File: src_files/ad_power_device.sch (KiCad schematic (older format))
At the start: 17 parts, among them J1 SPEAKER, J2 5622-6309-ML, Q1 DTC143ZEBTL, Q2 DTC143ZEBTL, U7 QUECTEL_L70-RL

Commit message: update NFC, 5G, GPS__left LiPo charger+screen changes
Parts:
- added C? (x3): 100nF, symbol Device:C_Small
- added C? (x2): 220pF, symbol Device:C_Small
- added C? (x2): 180pF, symbol Device:C_Small
- added C?: 66pF, symbol Device:C_Small
- added C?: 4.7uF, symbol Device:C_Small
- added J?: Conn_01x05_Male, symbol Connector:Conn_01x05_Male
- added J?: 205957-0271, 2059570271, symbol SamacSys_Parts:205957-0271
- added R? (x2): 0R, Resistor_SMD:R_0402_1005Metric, symbol Device:R_US
- added R? (x2): 4.7K, Resistor_SMD:R_0402_1005Metric, symbol Device:R_US
- added R?: 1K, Resistor_SMD:R_0402_1005Metric, symbol Device:R_US
- added U?: NFC_VS1797SM, greencharge-footprints:VS1797SM, symbol GCL_Integrated-Circuits:NFC_VS1797SM
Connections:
- net labels added: ANTRDR_n, ANTRDR_p, NFC_REQ, NFC_SCL, NFC_SDA, NFC_WAKE, PWM_IR, RF1, RF2, RX_IR, TX_IR, VCC3V3_PMU, VDDIO
- wire segments 189 -> 277
- no-connect marks 13 -> 18
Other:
- note added: "5G_RADAR_MODULE\n"
- note added: "ANTENNA CONNECTOR"
- note added: "I2C_PULLUP"
- note added: "NFC_IC_VS1797SM"
- note added: "NFC_MODULE SECTION"
- note added: "NOTE: accompanying NFC ANTENNA\n538-146236-2151\nlink: https://eu.mouser.com/ProductDetail/Molex/146236-2151?qs=xZ%2FP%252Ba9zWqYI0Z0ju1H6Kw%3D%3D"
- note added: "TO 5G RADA MODULE"
- note added: "https://www.hlktech.com/en/Product/Details/85"
- moved on the sheet: H1, H2, H3, H4

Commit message: schematic capture complete
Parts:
- removed AE2: Antenna, symbol Device:Antenna
- added C283: 100nF, Capacitor_SMD:C_0402_1005Metric, symbol Device:C_Small
- added J15: U.FL-R-SMT-1(10), greencharge-footprints:HRS_U.FL-R-SMT-1(10), symbol U.FL-R-SMT-1_10_:U.FL-R-SMT-1(10)
- C149, C150: footprint (none) -> Capacitor_SMD:C_0402_1005Metric
- C177, C178, C179, C180, C181, C182, C183, C184, C185: renamed from C?; footprint (none) -> Capacitor_SMD:C_0402_1005Metric
- D1, D2: footprint LED_SMD:LED_0402_1005Metric -> LED_SMD:LED_0201_0603Metric_Pad0.64x0.40mm_HandSolder
- J3: renamed from J?; footprint 2059570271 -> greencharge-footprints:2059570271
- J7: renamed from J?; footprint (none) -> Connector_PinHeader_2.54mm:PinHeader_1x05_P2.54mm_Vertical
- R28: footprint (none) -> Resistor_SMD:R_0402_1005Metric
- gave numbers to parts that had none: 6
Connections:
- net labels added: I2C0_SCL_PMIC, I2C0_SDA_PMIC, PMIC_EXT_EN, RECOVER, USB_OTG0_D+, USB_OTG0_D-, USB_OTG0_VBUSDET, VCC3V3_EXT
- net labels removed: VCC3V3_PMU
- wire segments 277 -> 308
- no-connect marks 18 -> 29
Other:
- note added: "RK3566 AND SUPPORTING COMPONENTS SECTION"
- note added: "USB_OTG AND POWER_INPUT"
- moved on the sheet: J1

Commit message: updated footprint and schematics
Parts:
- removed C149: 10uF, Capacitor_SMD:C_0402_1005Metric, symbol Device:C_Small
- removed C150, C283: 100nF, Capacitor_SMD:C_0402_1005Metric, symbol Device:C_Small
- removed D1, D2: LED, LED_SMD:LED_0201_0603Metric_Pad0.64x0.40mm_HandSolder, symbol Device:LED
- removed J15: U.FL-R-SMT-1(10), greencharge-footprints:HRS_U.FL-R-SMT-1(10), symbol U.FL-R-SMT-1_10_:U.FL-R-SMT-1(10)
- removed Q1, Q2: DTC143ZEBTL, greencharge-footprints:SOTFL50P160X85-3N, symbol DTC143ZEBTL:DTC143ZEBTL
- removed R28: 0R, Resistor_SMD:R_0402_1005Metric, symbol Device:R_US
- removed R29, R30: 1K, Resistor_SMD:R_0402_1005Metric, symbol Device:R_US
- removed U7: QUECTEL_L70-RL, greencharge-footprints:QUECTEL_L70-R, symbol GCL_Integrated-Circuits:QUECTEL_L70-R
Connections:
- net labels added: AP_READY
- net labels removed: +3V3, IPPS, STANDBY
- wire segments 308 -> 268
- no-connect marks 29 -> 23
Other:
- note added: "4G AND GPS_MODULE(COMPACT)\n"
- note added: "LINK TO DRIVE SATA TYPE: \nhttps://de.aliexpress.com/item/4001072133790.html?spm=a2g0o.detail.1000014.15.36804d48TZzJhy&gps-id=pcDetailBottomMoreOtherSeller&scm=1007.33416.213724.0&scm_id=1007.33416.213724.0&scm-url=1007.33416.213724.0&pvid=9e456f25-bf32-4544-9c19-67c56a9949ae&_t=gps-id:pcDetailBottomMoreOtherSeller,scm-url:1007.33416.213724.0,pvid:9e456f25-bf32-4544-9c19-67c56a9949ae,tpp_buckets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"
- note removed: "4G_MODULE\n"
- note removed: "GPS_MODULE"
- note removed: "Z0=50Ohm\n"

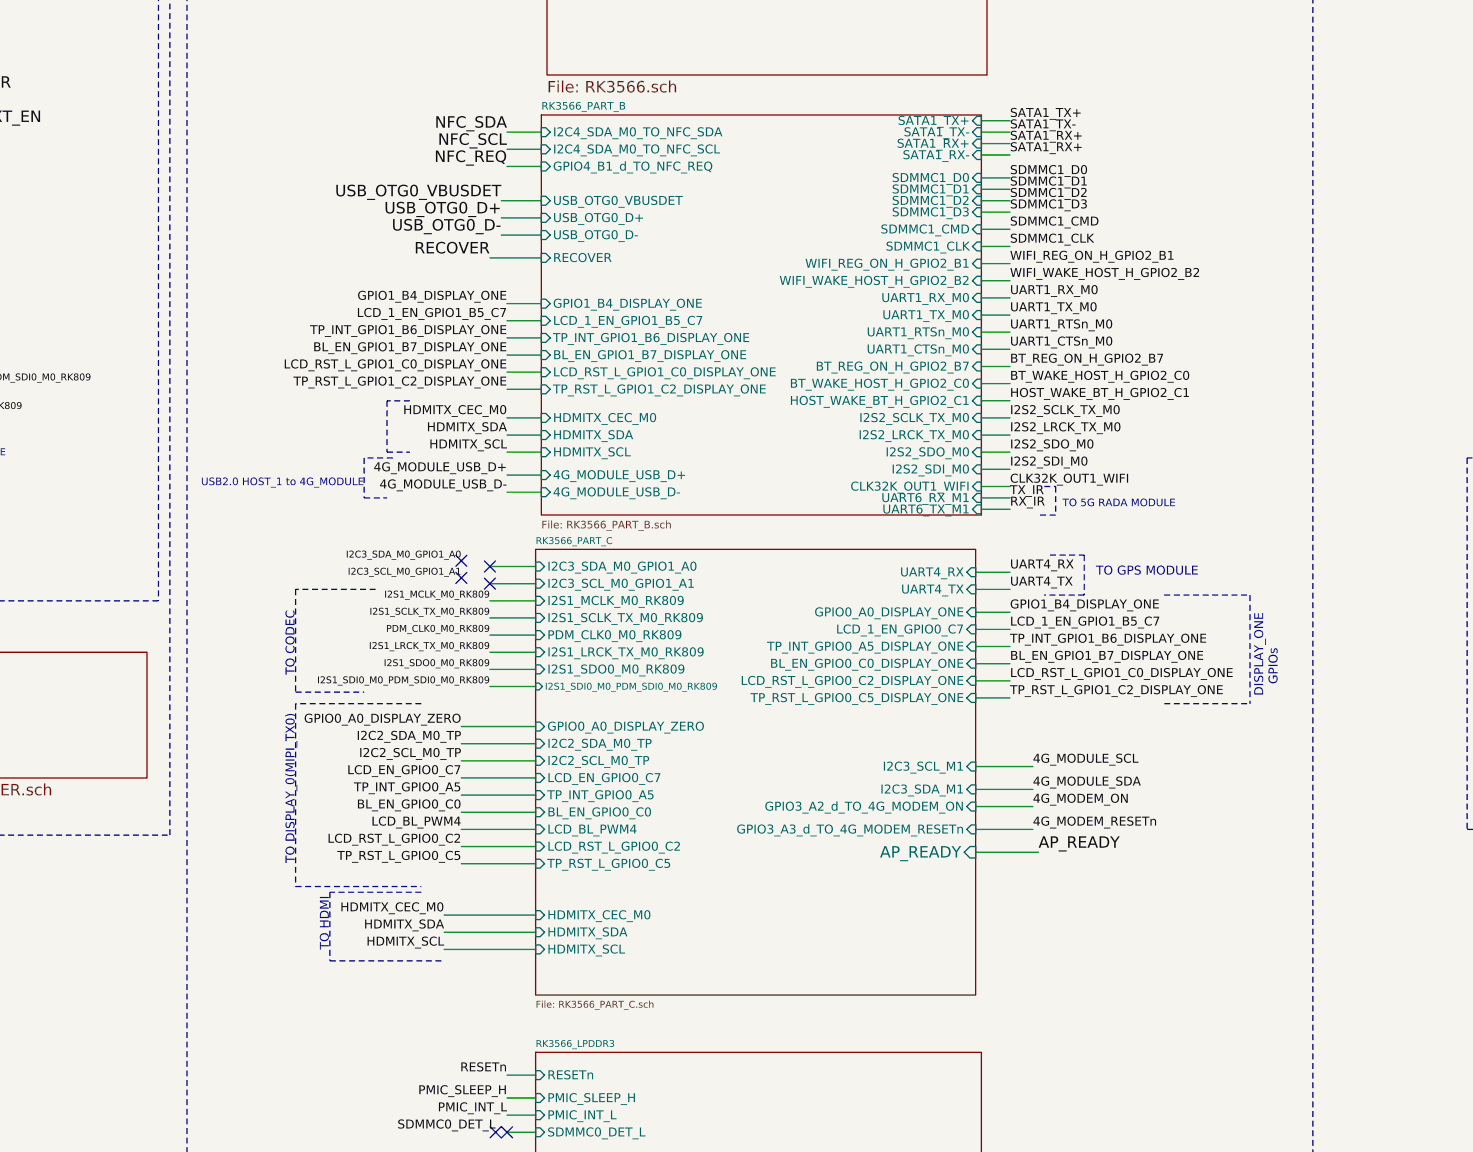
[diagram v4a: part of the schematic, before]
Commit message: complete update on schematic and all display interfaces
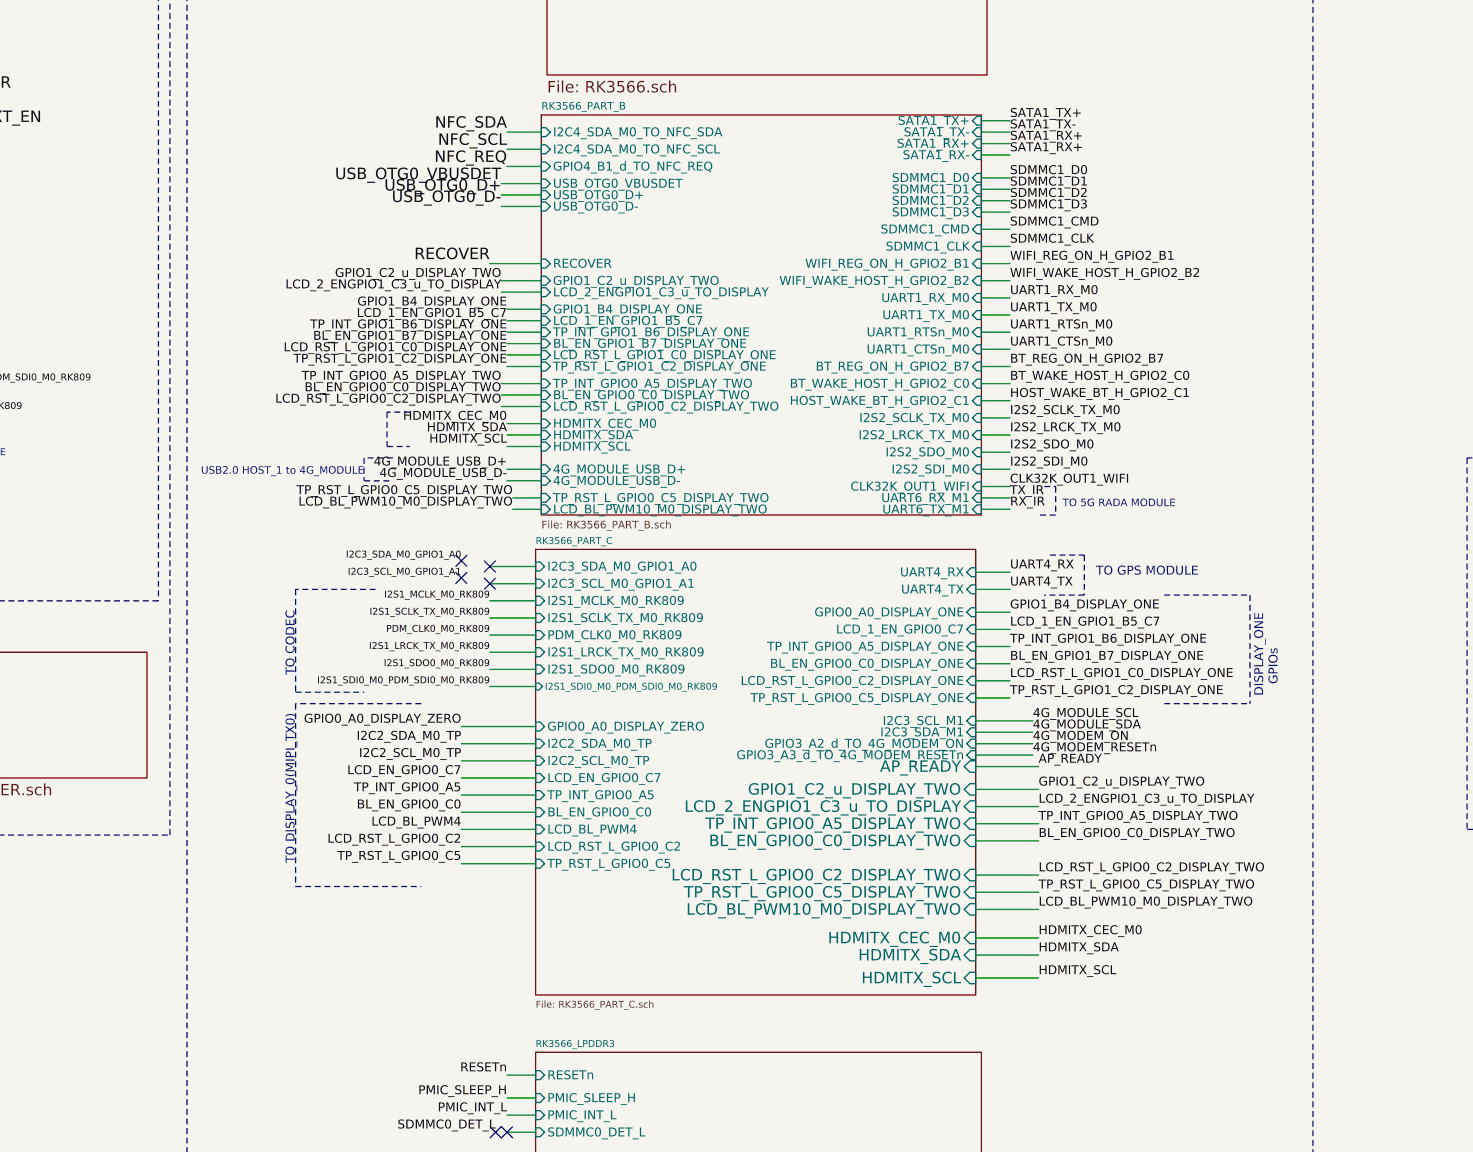
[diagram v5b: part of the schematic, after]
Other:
- note removed: "TO HDMI"

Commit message: complete update on schematiC + FOOTPRINT
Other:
- note removed: "TO GPS MODULE"
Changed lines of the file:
@@
 Wire Notes Line
 	4650 625  6575 625
-Text Label 10300 4325 0    39   ~ 0
-UART4_RX
-Text Label 10300 4400 0    39   ~ 0
-UART4_TX
-Wire Wire Line
-	10150 4325 10300 4325
-Wire Wire Line
-	10150 4400 10300 4400
 $Comp
 L Mechanical:MountingHole H1
@@
 F2 "PMIC_EXT_EN" I R 4450 4825 39
 $EndSheet
-Text Notes 11125 4350 2    39   ~ 0
-TO GPS MODULE
-Wire Notes Line
-	10625 4425 10450 4425
-Wire Notes Line
-	10625 4250 10625 4425
-Wire Notes Line
-	10475 4250 10625 4250
 Wire Notes Line
 	10975 4425 11350 4425
@@
 F8 "I2S1_SDO0_M0_RK809" I L 8225 4750 39
 F9 "I2S1_SDI0_M0_PDM_SDI0_M0_RK809" I L 8225 4825 30
-F10 "UART4_RX" I R 10150 4325 39
-F11 "UART4_TX" I R 10150 4400 39
-F12 "GPIO0_A0_DISPLAY_ZERO" I L 8225 5000 39
-F13 "I2C2_SDA_M0_TP" I L 8225 5075 39
-F14 "I2C2_SCL_M0_TP" I L 8225 5150 39
-F15 "LCD_EN_GPIO0_C7" I L 8225 5225 39
-F16 "TP_INT_GPIO0_A5" I L 8225 5300 39
-F17 "BL_EN_GPIO0_C0" I L 8225 5375 39
-F18 "LCD_BL_PWM4" I L 8225 5450 39
-F19 "LCD_RST_L_GPIO0_C2" I L 8225 5525 39
-F20 "TP_RST_L_GPIO0_C5" I L 8225 5600 39
-F21 "GPIO0_A0_DISPLAY_ONE" I R 10150 4500 39
-F22 "LCD_1_EN_GPIO0_C7" I R 10150 4575 39
-F23 "TP_INT_GPIO0_A5_DISPLAY_ONE" I R 10150 4650 39
-F24 "BL_EN_GPIO0_C0_DISPLAY_ONE" I R 10150 4725 39
-F25 "LCD_RST_L_GPIO0_C2_DISPLAY_ONE" I R 10150 4800 39
-F26 "TP_RST_L_GPIO0_C5_DISPLAY_ONE" I R 10150 4875 39
-F27 "I2C3_SCL_M1" I R 10150 4975 39
-F28 "I2C3_SDA_M1" I R 10150 5025 39
-F29 "GPIO3_A2_d_TO_4G_MODEM_ON" I R 10150 5075 39
-F30 "GPIO3_A3_d_TO_4G_MODEM_RESETn" I R 10150 5125 39
-F31 "AP_READY" I R 10150 5175 50
-F32 "GPIO1_C2_u_DISPLAY_TWO" I R 10150 5275 50
-F33 "LCD_2_ENGPIO1_C3_u_TO_DISPLAY" I R 10150 5350 50
-F34 "TP_INT_GPIO0_A5_DISPLAY_TWO" I R 10150 5425 50
-F35 "BL_EN_GPIO0_C0_DISPLAY_TWO" I R 10150 5500 50
-F36 "LCD_RST_L_GPIO0_C2_DISPLAY_TWO" I R 10150 5650 50
-F37 "TP_RST_L_GPIO0_C5_DISPLAY_TWO" I R 10150 5725 50
-F38 "LCD_BL_PWM10_M0_DISPLAY_TWO" I R 10150 5800 50
-F39 "HDMITX_CEC_M0" I R 10150 5925 50
-F40 "HDMITX_SDA" I R 10150 6000 50
-F41 "HDMITX_SCL" I R 10150 6100 50
+F10 "GPIO0_A0_DISPLAY_ZERO" I L 8225 5000 39
+F11 "I2C2_SDA_M0_TP" I L 8225 5075 39
+F12 "I2C2_SCL_M0_TP" I L 8225 5150 39
+F13 "LCD_EN_GPIO0_C7" I L 8225 5225 39
+F14 "TP_INT_GPIO0_A5" I L 8225 5300 39
+F15 "BL_EN_GPIO0_C0" I L 8225 5375 39
+F16 "LCD_BL_PWM4" I L 8225 5450 39
+F17 "LCD_RST_L_GPIO0_C2" I L 8225 5525 39
+F18 "TP_RST_L_GPIO0_C5" I L 8225 5600 39
+F19 "GPIO0_A0_DISPLAY_ONE" I R 10150 4500 39
+F20 "LCD_1_EN_GPIO0_C7" I R 10150 4575 39
+F21 "TP_INT_GPIO0_A5_DISPLAY_ONE" I R 10150 4650 39
+F22 "BL_EN_GPIO0_C0_DISPLAY_ONE" I R 10150 4725 39
+F23 "LCD_RST_L_GPIO0_C2_DISPLAY_ONE" I R 10150 4800 39
+F24 "TP_RST_L_GPIO0_C5_DISPLAY_ONE" I R 10150 4875 39
+F25 "I2C3_SCL_M1" I R 10150 4975 39
+F26 "I2C3_SDA_M1" I R 10150 5025 39
+F27 "GPIO3_A2_d_TO_4G_MODEM_ON" I R 10150 5075 39
+F28 "GPIO3_A3_d_TO_4G_MODEM_RESETn" I R 10150 5125 39
+F29 "AP_READY" I R 10150 5175 50
+F30 "GPIO1_C2_u_DISPLAY_TWO" I R 10150 5275 50
+F31 "LCD_2_ENGPIO1_C3_u_TO_DISPLAY" I R 10150 5350 50
+F32 "TP_INT_GPIO0_A5_DISPLAY_TWO" I R 10150 5425 50
+F33 "BL_EN_GPIO0_C0_DISPLAY_TWO" I R 10150 5500 50
+F34 "LCD_RST_L_GPIO0_C2_DISPLAY_TWO" I R 10150 5650 50
+F35 "TP_RST_L_GPIO0_C5_DISPLAY_TWO" I R 10150 5725 50
+F36 "LCD_BL_PWM10_M0_DISPLAY_TWO" I R 10150 5800 50
+F37 "HDMITX_CEC_M0" I R 10150 5925 50
+F38 "HDMITX_SDA" I R 10150 6000 50
+F39 "HDMITX_SCL" I R 10150 6100 50
 $EndSheet
 Text Label 10425 5275 0    39   ~ 0

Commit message: wireless power TX RX added
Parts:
- removed J1: SPEAKER, Connector_JST:JST_EH_B2B-EH-A_1x02_P2.50mm_Vertical, symbol Connector:Conn_01x02_Male
- added TP28: SPK-, TestPoint:TestPoint_Pad_1.5x1.5mm, symbol Connector:TestPoint
- added TP29: SPK+, TestPoint:TestPoint_Pad_1.5x1.5mm, symbol Connector:TestPoint
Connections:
- net RK809_CODEC/SPK_MINI_N: now also TP28.1
- net RK809_CODEC/SPK_MINI_P: now also TP29.1
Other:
- note added: "WIRELESS POWER TX"
- note added: "WIRELESS Qi POWER_INPUT"
- note removed: "SPEAKER OUT\n"
- note removed: "USB_OTG AND POWER_INPUT"
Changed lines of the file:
@@
 $Descr A3 16535 11693
 encoding utf-8
-Sheet 1 15
+Sheet 1 16
 Title ""
 Date ""
@@
 Text Notes 5575 3875 0    30   ~ 0
 TO HEADPHONE \n    JACK
-$Comp
-L Connector:Conn_01x02_Male J1
-U 1 1 61D2168A
-P 3400 4300
-F 0 "J1" V 3400 4400 50  0000 C CNN
-F 1 "SPEAKER" V 3300 4275 50  0000 C CNN
-F 2 "Connector_JST:JST_EH_B2B-EH-A_1x02_P2.50mm_Vertical" H 3400 4300 50  0001 C CNN
-F 3 "~" H 3400 4300 50  0001 C CNN
-	1    3400 4300
-	0    1    -1   0
-$EndComp
 Wire Wire Line
 	3725 3925 3400 3925
@@
 Wire Wire Line
 	3300 3850 3725 3850
-Text Notes 3750 4250 2    30   ~ 0
-SPEAKER OUT\n
 Text Label 8100 6625 2    39   ~ 0
 PMIC_SLEEP_H
@@
 Wire Wire Line
 	1650 1050 1575 1050
-Text Notes 1850 600  2    50   ~ 10
-USB_OTG AND POWER_INPUT
+Text Notes 1825 600  2    50   ~ 10
+WIRELESS Qi POWER_INPUT
 Wire Notes Line rgb(194, 65, 67)
 	775  550  525  550
@@
 Wire Wire Line
 	10425 6100 10150 6100
+$Sheet
+S 13325 8675 2215 730
+U 626A6204
+F0 "5W_QI_PWR_OUTPUT" 50
+F1 "5W_QI_PWR_OUTPUT.sch" 50
+$EndSheet
+$Comp
+L Connector:TestPoint TP?
+U 1 1 631A0D75
+P 3400 4100
+AR Path="/626A6204/631A0D75" Ref="TP?"  Part="1"
+AR Path="/631A0D75" Ref="TP29"  Part="1"
+F 0 "TP29" H 3210 4295 50  0000 L CNN
+F 1 "SPK+" H 3125 4220 50  0000 L CNN
+F 2 "TestPoint:TestPoint_Pad_1.5x1.5mm" H 3600 4100 50  0001 C CNN
+F 3 "https://kimchen8.en.made-in-china.com/product/pvWQfngkJchS/China-Qi-Wireless-Charger-Transmitter-6-3-Uh-Coil-for-Mobile-Phone.html" H 3600 4100 50  0001 C CNN
+F 4 "" V 3400 4100 50  0001 C CNN "Field4"
+	1    3400 4100
+	-1   0    0    1
+$EndComp
+$Comp
+L Connector:TestPoint TP?
+U 1 1 631A0D7C
+P 3300 4100
+AR Path="/626A6204/631A0D7C" Ref="TP?"  Part="1"
+AR Path="/631A0D7C" Ref="TP28"  Part="1"
+F 0 "TP28" H 3380 4275 50  0000 L CNN
+F 1 "SPK-" H 3325 4200 50  0000 L CNN
+F 2 "TestPoint:TestPoint_Pad_1.5x1.5mm" H 3500 4100 50  0001 C CNN
+F 3 "https://kimchen8.en.made-in-china.com/product/pvWQfngkJchS/China-Qi-Wireless-Charger-Transmitter-6-3-Uh-Coil-for-Mobile-Phone.html" H 3500 4100 50  0001 C CNN
+F 4 "" V 3300 4100 50  0001 C CNN "Field4"
+	1    3300 4100
+	-1   0    0    1
+$EndComp
+Wire Notes Line
+	15825 8300 15825 9775
+Wire Notes Line
+	15825 9775 12900 9775
+Wire Notes Line
+	12900 9775 12900 8300
+Wire Notes Line
+	12900 8300 15825 8300
+Text Notes 12925 8425 0    50   ~ 0
+WIRELESS POWER TX
 $EndSCHEMATC
